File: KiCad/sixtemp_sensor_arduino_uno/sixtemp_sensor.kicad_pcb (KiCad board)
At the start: 2 copper layers, 53.3 x 68.6 mm, 46 parts, among them J1 Conn_Led_1, J2 Conn_Led_2, J3 Conn_Led_2, J4 Conn_Led_3, J5 Conn_Led_5, J6 Conn_Led_6, J7 I2C, J71 Temp1, J72 Temp2, J73 Temp3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

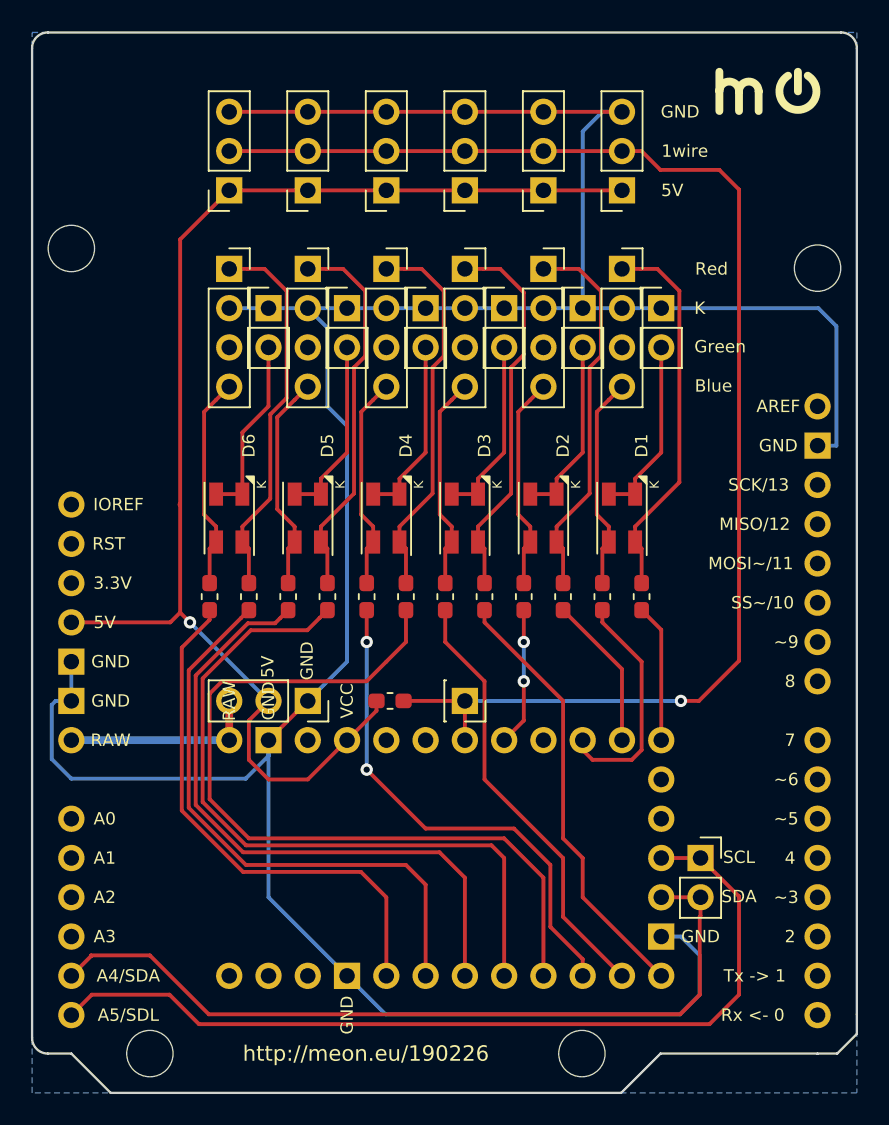
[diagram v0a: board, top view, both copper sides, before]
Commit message: adapt to 3x new pins and spacial reorganization
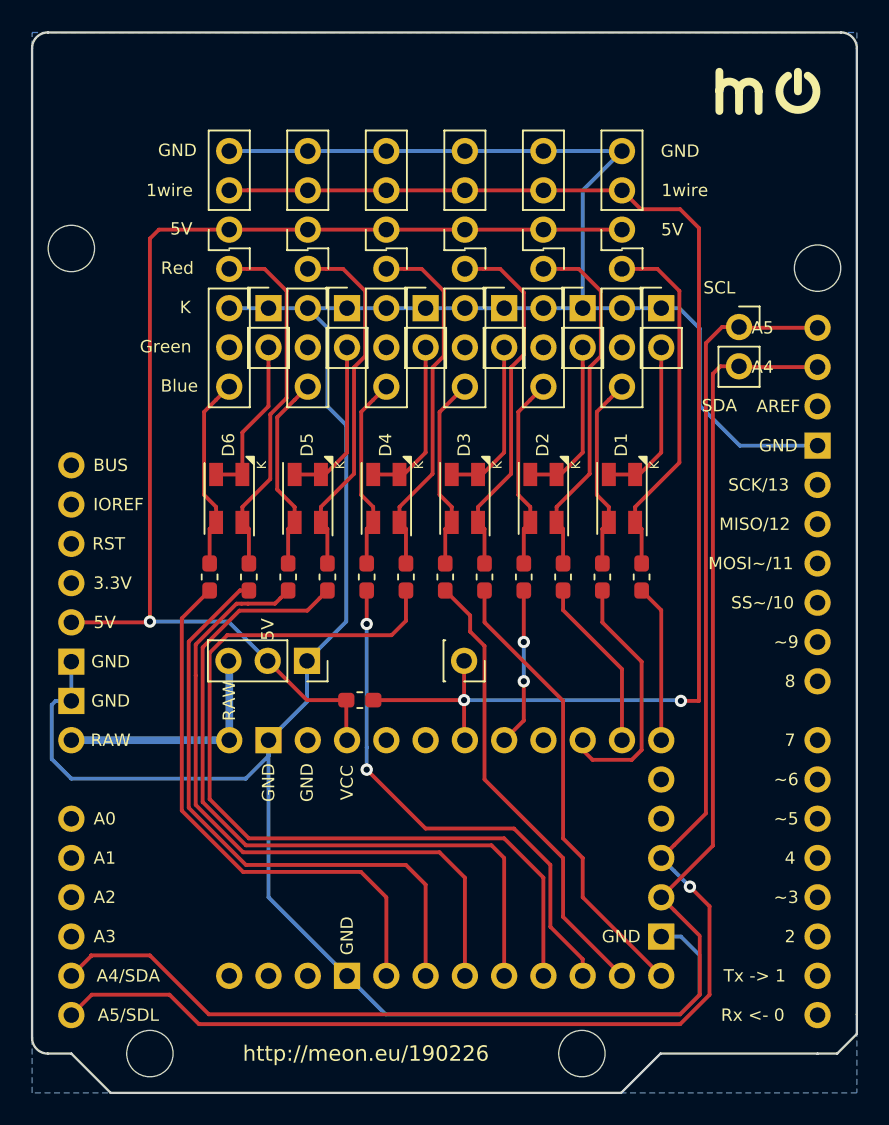
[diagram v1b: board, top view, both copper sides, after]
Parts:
- moved J7 34.4 mm to (111.8, 52.1)
- moved J9 2.59 mm to (83.8, 73.7)
- moved J8 2.59 mm to (94.0, 73.7)
- moved J71 2.54 mm to (104.2, 45.8)
- moved J72 2.54 mm to (99.1, 45.8)
- moved J73 2.54 mm to (94.0, 45.8)
- moved J74 2.54 mm to (83.9, 45.8)
- moved J75 2.54 mm to (89.0, 45.8)
- moved J76 2.54 mm to (78.8, 45.8)
- moved R101 1.96 mm to (87.2, 76.2)
- moved D1 1.27 mm to (104.2, 63.2)
- moved D2 1.27 mm to (99.1, 63.2)
- moved D3 1.27 mm to (94.0, 63.2)
- moved D4 1.27 mm to (89.0, 63.2)
- moved D5 1.27 mm to (83.9, 63.2)
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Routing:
- net SDA: track 52.2 -> 92.3 mm
- net SCL: track 57.7 -> 95.3 mm, vias 0 -> 1
- net GND: track 190.5 -> 183.1 mm
- net +5V: track 85.1 -> 78.1 mm
- net RAW: track 12.8 -> 15.4 mm
- net Net-(R41-Pad2): track 53.0 -> 55.0 mm
- net Net-(R52-Pad2): track 41.8 -> 43.5 mm
- net Net-(R51-Pad2): track 46.5 -> 48.2 mm
- net 1wire: track 89.8 -> 88.1 mm, vias 1 -> 2
- net Net-(R61-Pad2): track 37.7 -> 39.3 mm
- net Net-(D3-Pad1): track 24.6 -> 23.4 mm
- net Net-(D6-Pad2): track 13.9 -> 12.6 mm
- net Net-(D4-Pad2): track 13.9 -> 12.6 mm
- net Net-(D2-Pad2): track 13.9 -> 12.6 mm
- net Net-(D1-Pad2): track 13.9 -> 12.6 mm
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
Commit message: schematics with dtr pin and sidewise dtr/txo/rxi
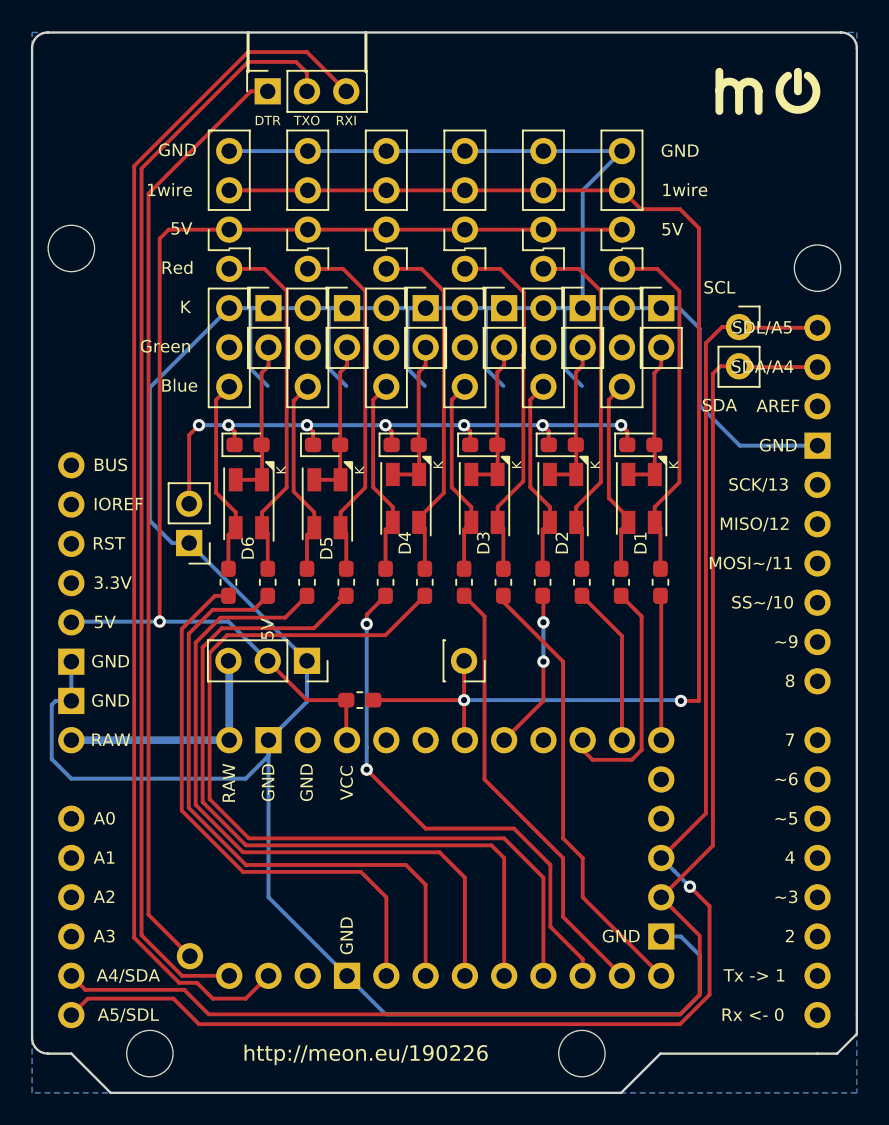
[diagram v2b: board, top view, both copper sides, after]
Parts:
- added D19: D, Diode_SMD:D_0603_1608Metric_Pad1.05x0.95mm_HandSolder, F.Cu at (105.4, 59.7)
- added D29: D, Diode_SMD:D_0603_1608Metric_Pad1.05x0.95mm_HandSolder, F.Cu at (100.3, 59.7)
- added D39: D, Diode_SMD:D_0603_1608Metric_Pad1.05x0.95mm_HandSolder, F.Cu at (95.2, 59.7)
- added D49: D, Diode_SMD:D_0603_1608Metric_Pad1.05x0.95mm_HandSolder, F.Cu at (90.2, 59.7)
- added D59: D, Diode_SMD:D_0603_1608Metric_Pad1.05x0.95mm_HandSolder, F.Cu at (85.1, 59.7)
- added D69: D, Diode_SMD:D_0603_1608Metric_Pad1.05x0.95mm_HandSolder, F.Cu at (80.0, 59.7)
- added J10: debug, Connector_PinSocket_2.54mm:PinSocket_1x03_P2.54mm_Vertical, F.Cu at (81.3, 36.8)
- added JP99: Jumper, Connector_PinHeader_2.54mm:PinHeader_1x02_P2.54mm_Vertical, F.Cu at (76.2, 66.0)
- U1: value Arduino_Pro_Mini_12_12_5 -> Arduino_Pro_Mini_12_12_5_1; footprint Arduino_Shields:Shield_Arduino_Pro_Mini_12+12+5_pins -> Arduino_Shields:Shield_Arduino_Pro_Mini_12+12+5+1_pins
- moved D5 1.32 mm to (85.1, 63.5)
- moved D6 1.32 mm to (80.1, 63.5)
- moved D1 1.27 mm to (105.5, 63.2)
- moved D2 1.27 mm to (100.4, 63.2)
- moved D3 1.27 mm to (95.3, 63.2)
- moved D4 1.27 mm to (90.2, 63.2)
- moved R11 1.27 mm to (106.7, 68.6)
- moved R12 1.27 mm to (104.1, 68.6)
- moved R22 1.27 mm to (99.1, 68.6)
- moved R32 1.27 mm to (94.0, 68.6)
- moved R41 1.27 mm to (91.4, 68.6)
- moved R42 1.27 mm to (88.9, 68.6)
- moved R51 1.27 mm to (86.4, 68.6)
- moved R61 1.27 mm to (81.3, 68.6)
- moved R21 1.27 mm to (101.6, 68.6)
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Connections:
- U2 pad 90: (no net) -> Net-(U2-Pad90)
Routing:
- net Net-(J10-Pad3): track 0.00 -> 78.7 mm
- net Net-(J10-Pad2): track 0.00 -> 71.4 mm
- net Net-(J10-Pad1): track 0.00 -> 60.9 mm
- net en_all_led: track 0.00 -> 41.2 mm, vias 0 -> 7
- net GND: track 183.1 -> 221.2 mm
- net Net-(R51-Pad2): track 48.2 -> 50.0 mm
- net Net-(R61-Pad2): track 39.3 -> 40.7 mm
- net Net-(R52-Pad2): track 43.5 -> 44.7 mm
- net SDA: track 92.3 -> 91.2 mm
- net Net-(R32-Pad2): track 29.7 -> 28.8 mm
- net Net-(R11-Pad2): track 10.2 -> 9.36 mm
- net Net-(R12-Pad2): track 16.3 -> 15.5 mm
- net Net-(R21-Pad2): track 11.3 -> 10.4 mm
- net Net-(R31-Pad2): track 29.7 -> 28.8 mm
- net Net-(D3-Pad3): track 10.9 -> 10.1 mm
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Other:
- board text added: "DTR"
- board text added: "RXI"
- board text added: "TXO"

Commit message: moving around pins
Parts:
- moved R101 36.9 mm to (106.7, 44.8), turned to 270 degrees
- moved J8 35.3 mm to (111.8, 43.2)
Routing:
- net 1wire: track 88.1 -> 82.9 mm
- net +5V: track 77.4 -> 78.5 mm
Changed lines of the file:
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@@
     (thickness 1.6)
     (drawings 52)
-    (tracks 373)
+    (tracks 378)
     (zones 0)
     (modules 54)
@@
   )
   (module Resistor_SMD:R_0603_1608Metric_Pad1.05x0.95mm_HandSolder (layer F.Cu)
-    (at 87.235 76.2 180)
+    (at 106.68 44.845 270)
     (descr "Resistor SMD 0603 (1608 Metric), square (rectangular) end terminal, IPC_7351 nominal with elongated pad for handsoldering. (Body size source: http://www.tortai-tech.com/upload/download/2011102023233369053.pdf), generated with kicad-footprint-generator")
     (tags "resistor handsolder")
     (attr smd)
-    (fp_text reference R101 (at 0 -1.43 180) (layer F.SilkS) hide
-      (effects (font (size 1 1) (thickness 0.15)))
-    )
-    (fp_text value 4k7 (at 0.24 1.905 90) (layer F.Fab)
-      (effects (font (size 0.8 0.8) (thickness 0.15)))
-    )
-    (fp_text user %R (at 0 0 180) (layer F.Fab)
+    (fp_text reference R101 (at 0 -1.43 270) (layer F.SilkS) hide
+      (effects (font (size 1 1) (thickness 0.15)))
+    )
+    (fp_text value 4k7 (at 0.24 1.905 180) (layer F.Fab)
+      (effects (font (size 0.8 0.8) (thickness 0.15)))
+    )
+    (fp_text user %R (at 0 0 270) (layer F.Fab)
       (effects (font (size 0.4 0.4) (thickness 0.06)))
     )
@@
     (fp_line (start -0.8 -0.4) (end 0.8 -0.4) (layer F.Fab) (width 0.1))
     (fp_line (start -0.8 0.4) (end -0.8 -0.4) (layer F.Fab) (width 0.1))
-    (pad 2 smd roundrect (at 0.875 0 180) (size 1.05 0.95) (layers F.Cu F.Paste F.Mask) (roundrect_rratio 0.25)
+    (pad 2 smd roundrect (at 0.875 0 270) (size 1.05 0.95) (layers F.Cu F.Paste F.Mask) (roundrect_rratio 0.25)
       (net 34 +5V))
-    (pad 1 smd roundrect (at -0.875 0 180) (size 1.05 0.95) (layers F.Cu F.Paste F.Mask) (roundrect_rratio 0.25)
+    (pad 1 smd roundrect (at -0.875 0 270) (size 1.05 0.95) (layers F.Cu F.Paste F.Mask) (roundrect_rratio 0.25)
       (net 33 1wire))
     (model ${KISYS3DMOD}/Resistor_SMD.3dshapes/R_0603_1608Metric.wrl
@@
   )
   (module Connector_PinSocket_2.54mm:PinSocket_1x01_P2.54mm_Vertical (layer F.Cu)
-    (at 93.98 73.66 270)
+    (at 111.76 43.18 270)
     (descr "Through hole straight socket strip, 1x01, 2.54mm pitch, single row (from Kicad 4.0.7), script generated")
     (tags "Through hole socket strip THT 1x01 2.54mm single row")
@@
     (effects (font (size 0.8 0.8) (thickness 0.2)))
   )
-  (gr_text 5V (at 107.442 45.770801) (layer F.SilkS)
+  (gr_text 5V (at 108.204 45.770801) (layer F.SilkS)
     (effects (font (size 0.8 0.8) (thickness 0.15)))
   )
-  (gr_text 1wire (at 108.254801 43.230801) (layer F.SilkS)
+  (gr_text 1wire (at 108.966 43.18) (layer F.SilkS)
     (effects (font (size 0.8 0.8) (thickness 0.15)))
   )
-  (gr_text GND (at 107.95 40.690801) (layer F.SilkS)
+  (gr_text GND (at 108.712 40.64) (layer F.SilkS)
     (effects (font (size 0.8 0.8) (thickness 0.15)))
   )
@@
   (segment (start 108.000801 76.250801) (end 108.000801 76.250801) (width 0.25) (layer F.Cu) (net 33))
   (via (at 108.000801 76.250801) (size 0.8) (drill 0.4) (layers F.Cu B.Cu) (net 33))
-  (segment (start 109.169199 76.250801) (end 108.000801 76.250801) (width 0.25) (layer F.Cu) (net 33))
-  (segment (start 93.98 73.66) (end 93.98 76.2) (width 0.25) (layer F.Cu) (net 33))
   (segment (start 93.98 76.2) (end 93.98 78.74) (width 0.25) (layer F.Cu) (net 33))
   (segment (start 93.98 76.2) (end 93.98 76.2) (width 0.25) (layer F.Cu) (net 33))
@@
   (segment (start 107.95 76.2) (end 108.000801 76.250801) (width 0.25) (layer B.Cu) (net 33))
   (segment (start 93.98 76.2) (end 107.95 76.2) (width 0.25) (layer B.Cu) (net 33))
-  (segment (start 88.11 76.2) (end 93.98 76.2) (width 0.25) (layer F.Cu) (net 33))
-  (segment (start 109.169199 76.250801) (end 109.169199 45.669199) (width 0.25) (layer F.Cu) (net 33))
-  (segment (start 109.169199 45.669199) (end 107.95 44.45) (width 0.25) (layer F.Cu) (net 33))
-  (segment (start 105.41 44.45) (end 104.190801 43.230801) (width 0.25) (layer F.Cu) (net 33))
-  (segment (start 107.95 44.45) (end 105.41 44.45) (width 0.25) (layer F.Cu) (net 33))
   (segment (start 79.992882 43.230801) (end 104.190801 43.230801) (width 0.25) (layer F.Cu) (net 33))
   (segment (start 78.790801 43.230801) (end 79.992882 43.230801) (width 0.25) (layer F.Cu) (net 33))
+  (segment (start 108.000801 76.250801) (end 109.169199 75.082403) (width 0.25) (layer F.Cu) (net 33))
+  (segment (start 109.169199 75.082403) (end 109.169199 46.459199) (width 0.25) (layer F.Cu) (net 33))
+  (segment (start 109.169199 46.459199) (end 109.169199 45.770801) (width 0.25) (layer F.Cu) (net 33))
+  (segment (start 104.93 43.97) (end 104.190801 43.230801) (width 0.25) (layer F.Cu) (net 33))
+  (segment (start 106.68 43.97) (end 104.93 43.97) (width 0.25) (layer F.Cu) (net 33))
+  (segment (start 109.169199 45.770801) (end 109.169199 44.653199) (width 0.25) (layer F.Cu) (net 33))
+  (segment (start 109.169199 44.653199) (end 108.458 43.942) (width 0.25) (layer F.Cu) (net 33))
+  (segment (start 108.43 43.97) (end 106.68 43.97) (width 0.25) (layer F.Cu) (net 33))
+  (segment (start 108.458 43.942) (end 108.43 43.97) (width 0.25) (layer F.Cu) (net 33))
+  (segment (start 110.286801 44.653199) (end 111.76 43.18) (width 0.25) (layer F.Cu) (net 33))
+  (segment (start 109.169199 44.653199) (end 110.286801 44.653199) (width 0.25) (layer F.Cu) (net 33))
   (segment (start 81.28 73.66) (end 83.82 76.2) (width 0.25) (layer F.Cu) (net 34))
-  (segment (start 83.82 76.2) (end 86.36 76.2) (width 0.25) (layer F.Cu) (net 34))
   (segment (start 86.36 78.74) (end 86.410801 78.790801) (width 0.25) (layer F.Cu) (net 34))
-  (segment (start 86.36 76.2) (end 86.36 78.74) (width 0.25) (layer F.Cu) (net 34))
   (segment (start 78.790801 45.770801) (end 104.190801 45.770801) (width 0.25) (layer F.Cu) (net 34))
   (segment (start 78.74 71.12) (end 74.295 71.12) (width 0.25) (layer B.Cu) (net 34))
@@
   (segment (start 74.295 46.355) (end 74.879199 45.770801) (width 0.25) (layer F.Cu) (net 34))
   (segment (start 74.295 71.12) (end 74.295 46.355) (width 0.25) (layer F.Cu) (net 34))
+  (segment (start 86.410801 78.790801) (end 83.82 76.2) (width 0.25) (layer F.Cu) (net 34))
+  (segment (start 104.241602 45.72) (end 104.190801 45.770801) (width 0.25) (layer F.Cu) (net 34))
+  (segment (start 106.68 45.72) (end 104.241602 45.72) (width 0.25) (layer F.Cu) (net 34))
   (segment (start 106.730801 54.592882) (end 106.730801 53.390801) (width 0.25) (layer F.Cu) (net 35))
   (segment (start 104.610801 61.605801) (end 106.310801 61.605801) (width 0.25) (layer F.Cu) (net 35))

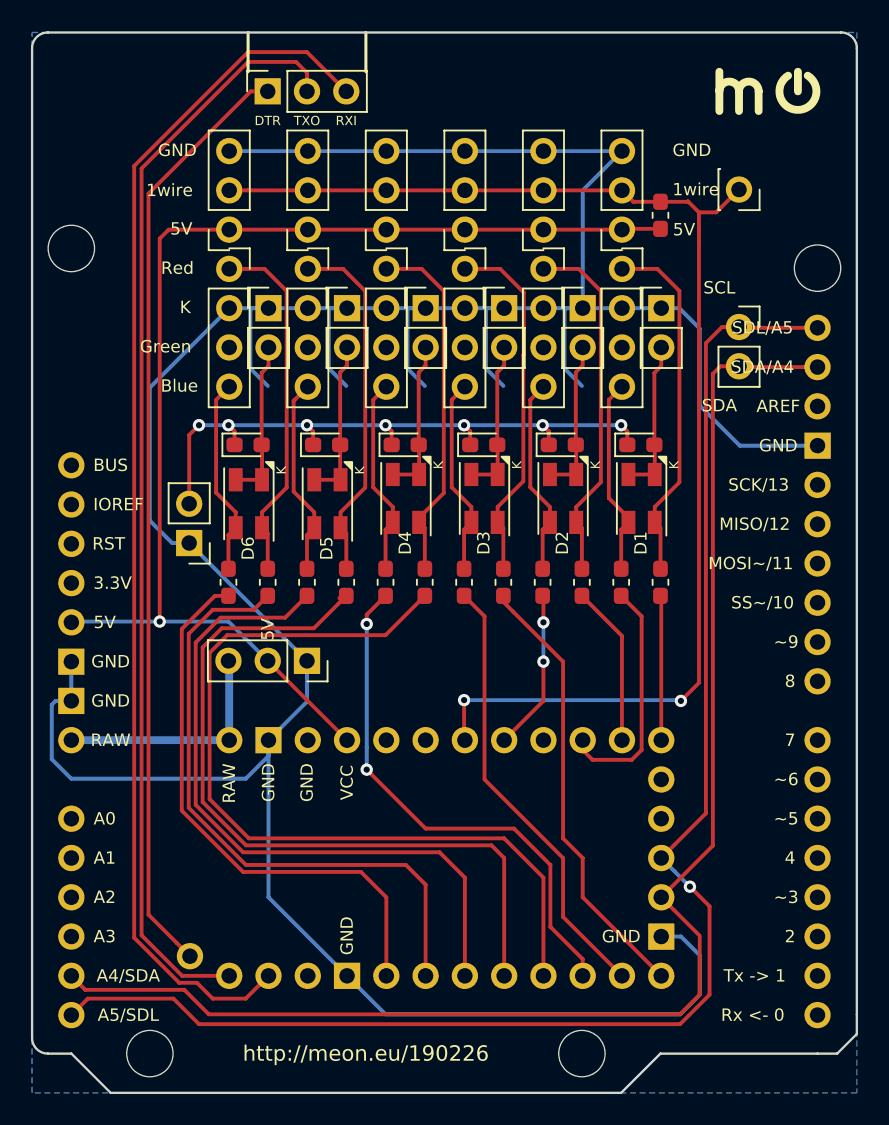
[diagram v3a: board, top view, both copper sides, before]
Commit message: connector for 2x6 pins, minimize via-s
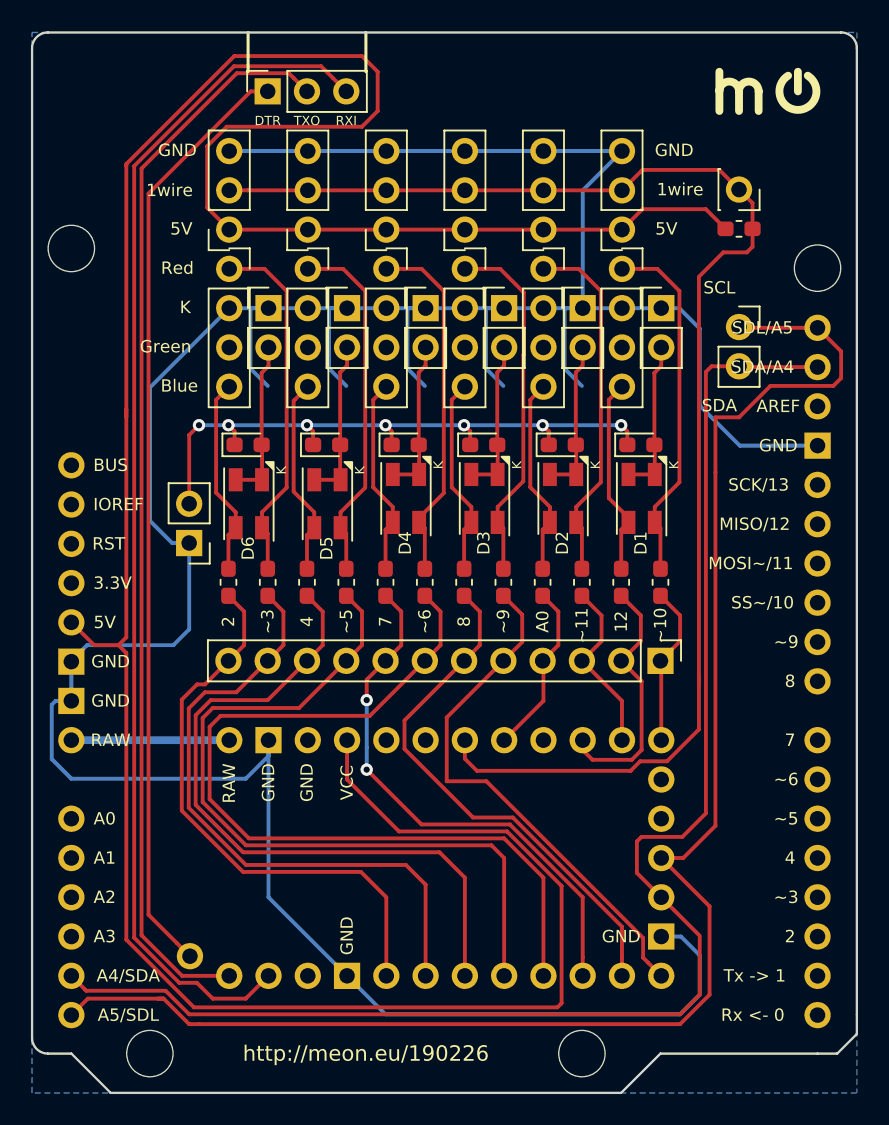
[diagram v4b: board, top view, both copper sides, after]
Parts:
- removed J9: Power, Connector_PinSocket_2.54mm:PinSocket_1x03_P2.54mm_Vertical
- added J12: Conn_01x12_Female, Connector_PinHeader_2.54mm:PinHeader_1x12_P2.54mm_Vertical, F.Cu at (106.7, 73.7)
- moved R101 5.15 mm to (111.8, 45.7), turned to 180 degrees
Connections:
- net Net-(R11-Pad2) renamed 10_~SS~~
- net Net-(R12-Pad2) renamed 12_MISO
- net Net-(R21-Pad2) renamed 11_MISO~~
- net Net-(R22-Pad2) renamed A0
- net Net-(R31-Pad2) renamed D9~~
- net Net-(R32-Pad2) renamed D8
- net Net-(R41-Pad2) renamed D6~~
- net Net-(R42-Pad2) renamed D7
- net Net-(R51-Pad2) renamed D5~~
- net Net-(R52-Pad2) renamed D4
- net Net-(R61-Pad2) renamed D3~~
- net Net-(R62-Pad2) renamed D2
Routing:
- net +5V: track 78.5 -> 185.1 mm, vias 1 -> 0
- net SCL: track 95.0 -> 102.2 mm, vias 1 -> 0
- net 1wire: track 82.9 -> 89.8 mm, vias 2 -> 0
- net D9~~: track 28.8 -> 34.8 mm
- net D8: track 28.8 -> 34.3 mm
- net RAW: track 15.4 -> 10.2 mm
- net SDA: track 91.2 -> 94.4 mm
- net GND: track 221.2 -> 218.3 mm
- net Net-(J10-Pad2): track 71.4 -> 70.1 mm
- net 10_~SS~~: track 9.36 -> 10.5 mm
- net 11_MISO~~: track 10.4 -> 11.5 mm
- net 12_MISO: track 15.5 -> 16.5 mm
- net A0: track 10.4 -> 11.4 mm, vias 2 -> 0
- net D7: track 34.2 -> 35.1 mm
- net Net-(J10-Pad3): track 78.7 -> 77.9 mm
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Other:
- board text added: "12"
- board text added: "2"
- board text added: "4"
- board text added: "7"
- board text added: "8"
- board text added: "A0"
- board text added: "~~10"
- board text added: "~~11"
- board text added: "~~3"
- board text added: "~~5"
- board text added: "~~6"
- board text added: "~~9"
